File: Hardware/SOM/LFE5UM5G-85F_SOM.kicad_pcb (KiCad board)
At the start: 6 copper layers, 67.6 x 25.4 mm, 131 parts, among them J1 SODIMM-200_Split, U1 LFE5UM5G-85F, U2 AS4C256M16D3, U3 W25Q128JVP, U4 TPS62A02ADRL, U5 TPS62A02ADRL, U6 TPS62A02ADRL, U7 TPS62A02ADRL

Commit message: SOM: layout update
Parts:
- added C100: 10uF, Capacitor_SMD:C_0402_1005Metric, F.Cu at (87.6, 67.3)
- added C101: 22uF, Capacitor_SMD:C_0805_2012Metric, F.Cu at (90.4, 71.4)
- added C102: 22uF, Capacitor_SMD:C_0805_2012Metric, F.Cu at (90.4, 67.2)
- added C83: 1uF, Capacitor_SMD:C_0402_1005Metric, F.Cu at (90.0, 32.4)
- added C84: 100nF, Capacitor_SMD:C_0402_1005Metric, F.Cu at (90.0, 34.4)
- added C85: 100nF, Capacitor_SMD:C_0402_1005Metric, F.Cu at (90.0, 36.4)
- added C86: 100nF, Capacitor_SMD:C_0402_1005Metric, F.Cu at (90.0, 38.3)
- added C87: 100nF, Capacitor_SMD:C_0402_1005Metric, F.Cu at (90.0, 40.3)
- added C88: 1uF, Capacitor_SMD:C_0402_1005Metric, F.Cu at (92.9, 32.4)
- added C89: 100nF, Capacitor_SMD:C_0402_1005Metric, F.Cu at (92.9, 34.4)
- added C90: 22pF, Capacitor_SMD:C_0402_1005Metric, F.Cu at (92.9, 36.4)
- added C91: 22pF, Capacitor_SMD:C_0402_1005Metric, F.Cu at (92.9, 38.3)
- added C92: 22pF, Capacitor_SMD:C_0402_1005Metric, F.Cu at (92.9, 40.3)
- added C93: 100nF, Capacitor_SMD:C_0402_1005Metric, F.Cu at (95.8, 32.4)
- added C94: 10uF, Capacitor_SMD:C_0402_1005Metric, F.Cu at (95.8, 34.4)
- added C95: 10uF, Capacitor_SMD:C_0402_1005Metric, F.Cu at (87.6, 79.5)
- added C96: 10uF, Capacitor_SMD:C_0402_1005Metric, F.Cu at (87.6, 75.5)
- added C97: 22uF, Capacitor_SMD:C_0805_2012Metric, F.Cu at (90.5, 79.4)
- added C98: 22uF, Capacitor_SMD:C_0805_2012Metric, F.Cu at (90.5, 75.5)
- added C99: 10uF, Capacitor_SMD:C_0402_1005Metric, F.Cu at (87.6, 71.4)
- added FB4: FerriteBead, Inductor_SMD:L_1206_3216Metric, F.Cu at (85.7, 33.1)
- added FB5: FerriteBead, Inductor_SMD:L_1206_3216Metric, F.Cu at (85.7, 36.6)
- added FB6: FerriteBead, Inductor_SMD:L_1206_3216Metric, F.Cu at (85.7, 40.0)
- added FB7: FerriteBead, Inductor_SMD:L_1206_3216Metric, F.Cu at (85.7, 43.5)
- added FB8: FerriteBead, Inductor_SMD:L_0402_1005Metric, F.Cu at (85.7, 47.0)
- added FB9: FerriteBead, Inductor_SMD:L_0402_1005Metric, F.Cu at (85.7, 50.4)
- C1, C14, C18, C22, C30, C31, C34, C35, C39, C5, C9: moved to B.Cu
- C40, C63: value 1uF -> 10uF
- C41, C42, C56, C57: value 100nF -> 10uF
- C44, C45: value 100nF -> 1uF
- C48, C68: value 1uF -> 100nF
- C54, C75, C76: value 10uF -> 100nF
- C55, C74, C80: value 10uF -> 1uF
- C58, C59: value 22uF -> 10uF; footprint Capacitor_SMD:C_0805_2012Metric -> Capacitor_SMD:C_0402_1005Metric
- C70, C72: value 22pF -> 1uF
- C71: value 22pF -> 100nF
- C77: value 22uF -> 100nF; footprint Capacitor_SMD:C_0805_2012Metric -> Capacitor_SMD:C_0402_1005Metric
- C79: value 10uF -> 22uF; footprint Capacitor_SMD:C_0402_1005Metric -> Capacitor_SMD:C_0805_2012Metric
- C81, C82: value 22uF -> 1uF; footprint Capacitor_SMD:C_0805_2012Metric -> Capacitor_SMD:C_0402_1005Metric
- FB2, FB3: footprint Inductor_SMD:L_0402_1005Metric -> Inductor_SMD:L_1206_3216Metric
- moved C30 76.0 mm to (115.5, 74.2), turned to 90 degrees
- moved C22 67.5 mm to (114.3, 68.9), turned to 90 degrees
- moved C31 66.6 mm to (115.3, 68.1), turned to -90 degrees
- moved C1 65.1 mm to (114.3, 70.9), turned to 90 degrees
- moved C9 64.6 mm to (117.5, 74.2), turned to 90 degrees
- moved C5 63.1 mm to (116.5, 74.2), turned to 90 degrees
- moved C14 62.1 mm to (117.1, 72.2), turned to -90 degrees
- moved C18 60.4 mm to (118.5, 72.4), turned to 180 degrees
- moved C39 56.5 mm to (118.4, 68.1), turned to -90 degrees
- moved C34 55.1 mm to (114.5, 74.2), turned to 90 degrees
- moved C35 55.1 mm to (115.6, 72.3), turned to 180 degrees
- moved C77 42.4 mm to (48.3, 75.1)
- moved C59 26.0 mm to (166.8, 55.0)
- moved FB2 24.0 mm to (158.6, 50.4)
- moved FB3 23.4 mm to (158.4, 53.5)
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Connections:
- C15 pad 2: Net-(C15-Pad2) -> 3.3V
- C19 pad 2: Net-(C15-Pad2) -> 3.3V
- C24 pad 2: Net-(C15-Pad2) -> 3.3V
- C40 pad 2: DDR_VREF -> VCCA0
- C41 pad 2: DDR_VREF -> VCCHTX0
- C42 pad 2: 2.5V_A -> VCC_SER_0
- C43 pad 2: DDR_VREF -> VCCA0
- C44 pad 2: 2.5V_A -> VCCHTX0
- C45 pad 2: DDR_VREF -> VCC_SER_0
- C47 pad 2: 2.5V_A -> VCCA0
- C48 pad 2: DDR_VREF -> VCCHTX0
- C49 pad 2: 2.5V_A -> VCC_SER_0
- C50 pad 2: DDR_VREF -> 2.5V_A
- C51 pad 2: 2.5V_A -> VCCA0
- C52 pad 2: 2.5V_A -> VCCHTX0
- C53 pad 2: 2.5V_A -> VCC_SER_0
- C56 pad 2: DDR_VDDQ_1.5V -> VCCA1
- C57 pad 2: DDR_VDD_1.5V -> VCCHTX1
- C58 pad 2: DDR_VDDQ_1.5V -> VCC_SER_1
- C59 pad 2: DDR_VDD_1.5V -> 2.5V_A
- C60 pad 2: DDR_VDDQ_1.5V -> VCCA1
- C61 pad 2: DDR_VDD_1.5V -> VCCHTX1
- C62 pad 2: DDR_VDDQ_1.5V -> VCC_SER_1
- C63 pad 2: DDR_VDD_1.5V -> 2.5V_A
- C64 pad 2: DDR_VDDQ_1.5V -> VCCA1
- C65 pad 2: DDR_VDD_1.5V -> VCCHTX1
- C66 pad 2: DDR_VDDQ_1.5V -> VCC_SER_1
- C67 pad 2: DDR_VDD_1.5V -> VCCA1
- C68 pad 2: DDR_VREF -> VCCHTX1
- C69 pad 2: DDR_VREF -> VCC_SER_1
- C70 pad 1: Net-(U3-~{CS}) -> GND
- C70 pad 2: GND -> DDR_VREF
- C71 pad 1: Net-(U3-CLK) -> GND
- C71 pad 2: GND -> DDR_VREF
- C72 pad 1: QSPI_MOSI/DQ0 -> GND
- C72 pad 2: GND -> DDR_VREF
- C73 pad 2: 3.3V -> DDR_VREF
- C74 pad 2: 3.3V -> DDR_VREF
- C75 pad 2: 5V -> DDR_VREF
- C76 pad 2: 5V -> DDR_VDDQ_1.5V
- C77 pad 2: 3.3V -> DDR_VDD_1.5V
- C78 pad 2: 2.5V -> DDR_VDDQ_1.5V
- C79 pad 2: 5V -> DDR_VDD_1.5V
- C80 pad 2: 5V -> DDR_VDDQ_1.5V
- C81 pad 2: 1.5V -> DDR_VDD_1.5V
- C82 pad 2: 1.2V -> DDR_VDDQ_1.5V
- FB1 pad 1: 2.5V -> 1.2V
- FB1 pad 2: 2.5V_A -> VCCA0
- FB2 pad 1: 1.5V -> 1.2V
- FB2 pad 2: DDR_VDDQ_1.5V -> VCCHTX0
- FB3 pad 1: 1.5V -> 1.2V
- FB3 pad 2: DDR_VDD_1.5V -> VCC_SER_0
- R1 pad 1: DDR_CKE -> /DDR/DDR_CKE
- R1 pad 2: DDR_NCK -> /DDR/DDR_NCK
- U1 pad F11: 1.5V -> 3.3V
- U1 pad F12: 1.5V -> 3.3V
- U1 pad F17: DDR_CKE -> DDR_CK_P
- U1 pad G18: DDR_NCK -> DDR_CK_N
- U1 pad T10: Net-(U1A-VCCHTX1_D0CH1) -> VCCHTX1
- U1 pad T11: Net-(U1A-VCCHTX0_D0CH0) -> VCCHTX0
- U1 pad T12: Net-(U1A-VCCHRX0_D0CH0) -> VCC_SER_0
- U1 pad T13: Net-(U1A-VCCHRX1_D0CH1) -> VCC_SER_1
- U1 pad T14: Net-(U1A-VCCHTX1_D0CH1) -> VCCHTX1
- U1 pad T15: 2.5V_A -> VCCA1
- U1 pad T6: 2.5V_A -> VCCA0
- U1 pad T7: Net-(U1A-VCCHTX0_D0CH0) -> VCCHTX0
- U1 pad T8: Net-(U1A-VCCHRX0_D0CH0) -> VCC_SER_0
- U1 pad T9: Net-(U1A-VCCHRX1_D0CH1) -> VCC_SER_1
- U1 pad U15: 2.5V_A -> VCCA1
- U1 pad U6: 2.5V_A -> VCCA0
- U2 pad K7: DDR_NCK -> DDR_CK_N
- U2 pad K9: DDR_CKE -> DDR_CK_P
- U5 pad 4: unconnected-(U5-EN-Pad4) -> /Power Supply/1.5V_PG
- U6 pad 4: unconnected-(U6-EN-Pad4) -> BB_PGOOD
- U6 pad 6: unconnected-(U6-PG-Pad6) -> /Power Supply/1.5V_PG
- U7 pad 4: unconnected-(U7-EN-Pad4) -> /Power Supply/1.5V_PG
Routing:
- net GND: track 90.9 -> 124.8 mm, vias 30 -> 62
- net 1.2V: track 2.04 -> 31.4 mm, vias 0 -> 12
- net DDR_UDQS_P: track 1.23 -> 24.3 mm
- net DDR_UDQS_N: track 1.23 -> 22.8 mm
- net DDR_LDQS_N: track 1.35 -> 21.5 mm
- net (no net): track 18.9 -> 0.00 mm, vias 3 -> 0
- net DDR_LDQS_P: track 1.36 -> 20.2 mm
- net DDR_DQ14: track 0.00 -> 18.2 mm, vias 0 -> 2
- net DDR_DQ8: track 0.00 -> 17.3 mm, vias 0 -> 2
- net DDR_DQ12: track 0.00 -> 17.2 mm
- net DDR_DQ9: track 0.00 -> 14.9 mm, vias 0 -> 2
- net DDR_DQ15: track 0.00 -> 14.4 mm, vias 0 -> 2
- net DDR_DQ13: track 0.00 -> 13.4 mm, vias 0 -> 3
- net DDR_DQ11: track 0.00 -> 13.4 mm, vias 0 -> 2
- net DDR_VREF: track 0.00 -> 12.6 mm, vias 0 -> 2
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- added copper zone on In4.Cu, net DDR_VDDQ_1.5V
- added copper zone on In4.Cu, net DDR_VDD_1.5V

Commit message: SOM: layout update
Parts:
- C46, C50, C54, C55, C59, C63, C72, C73, C74, C75: moved to B.Cu
- moved C77 95.6 mm to (143.9, 74.1), turned to 180 degrees
- moved C71 78.8 mm to (127.5, 62.7), turned to -90 degrees
- moved C70 77.8 mm to (126.4, 62.7), turned to -90 degrees
- moved C79 73.1 mm to (144.5, 75.7)
- moved C74 72.3 mm to (120.5, 74.3), turned to 90 degrees
- moved C78 70.3 mm to (144.5, 69.7), turned to 180 degrees
- moved C80 68.6 mm to (143.8, 68.2)
- moved R9 68.0 mm to (130.4, 70.6), turned to 180 degrees
- moved FB2 66.9 mm to (94.8, 70.5)
- moved R10 65.2 mm to (128.8, 69.1), turned to -90 degrees
- moved C82 65.2 mm to (139.9, 62.2), turned to 180 degrees
- moved FB3 65.2 mm to (94.8, 67.9)
- moved C72 64.5 mm to (112.7, 69.4), turned to -90 degrees
- moved C83 64.0 mm to (143.8, 67.1), turned to 180 degrees
- moved C73 62.7 mm to (111.2, 69.4), turned to -90 degrees
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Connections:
- J1 pad 10: unconnected-(J1-Pad10) -> 5V
- J1 pad 14: unconnected-(J1-Pad14) -> GND
- J1 pad 16: unconnected-(J1-Pad16) -> GND
- J1 pad 18: unconnected-(J1-Pad18) -> GND
- J1 pad 2: unconnected-(J1-Pad2) -> 5V
- J1 pad 20: unconnected-(J1-Pad20) -> GND
- J1 pad 22: unconnected-(J1-Pad22) -> GND
- J1 pad 4: unconnected-(J1-Pad4) -> 5V
- J1 pad 6: unconnected-(J1-Pad6) -> 5V
- J1 pad 8: unconnected-(J1-Pad8) -> 5V
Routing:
- net GND: track 124.8 -> 188.2 mm, vias 62 -> 97
- net 5V: track 32.5 -> 48.6 mm, vias 0 -> 10
- net DDR_VDDQ_1.5V: track 12.0 -> 26.5 mm
- net DDR_VREF: track 12.6 -> 26.8 mm, vias 2 -> 4
- net DDR_VDD_1.5V: track 11.0 -> 20.8 mm, vias 5 -> 4
- net 2.5V_A: track 0.57 -> 9.63 mm, vias 1 -> 6
- net 2.5V: track 2.03 -> 3.94 mm
- net VCCA1: track 0.00 -> 0.80 mm
- net VCCA0: track 0.00 -> 0.80 mm
- added copper zone on F.Cu, net 5V
- added copper zone on F.Cu, net GND

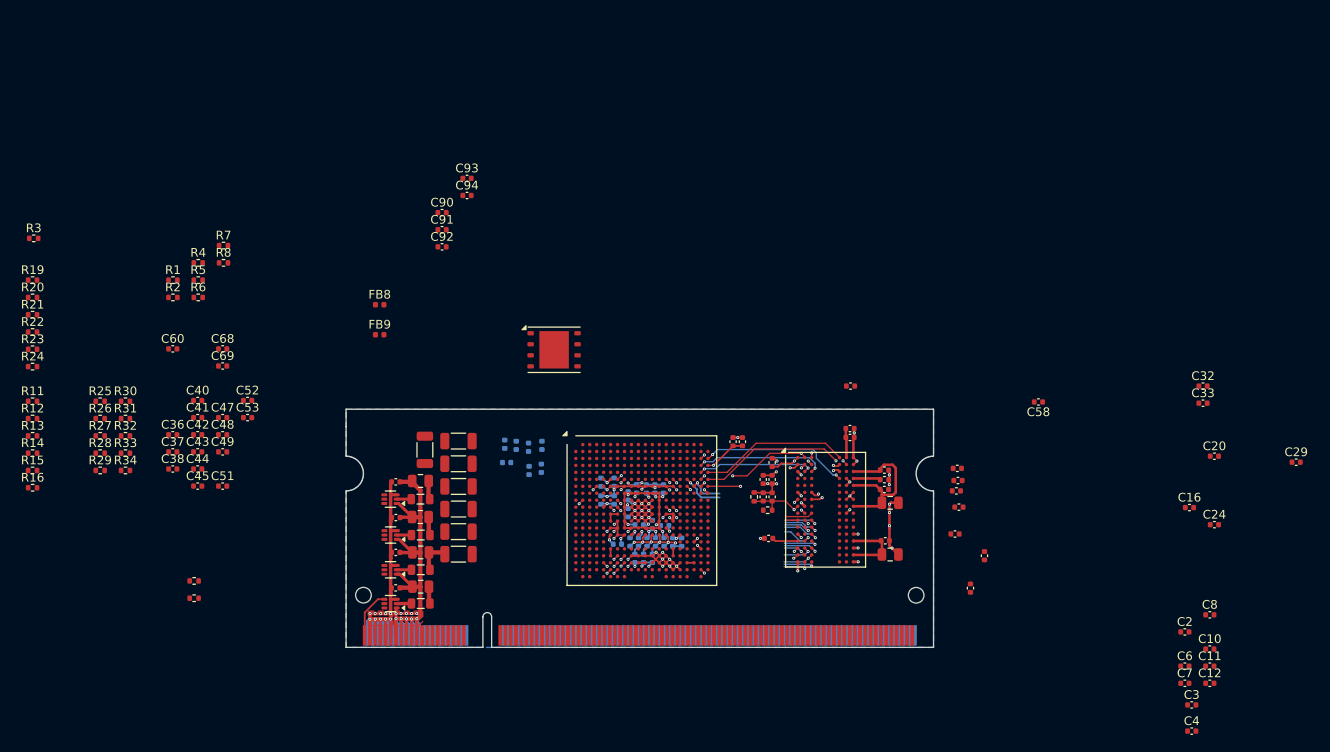
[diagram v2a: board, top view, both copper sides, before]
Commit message: SOM: QSPI layout update
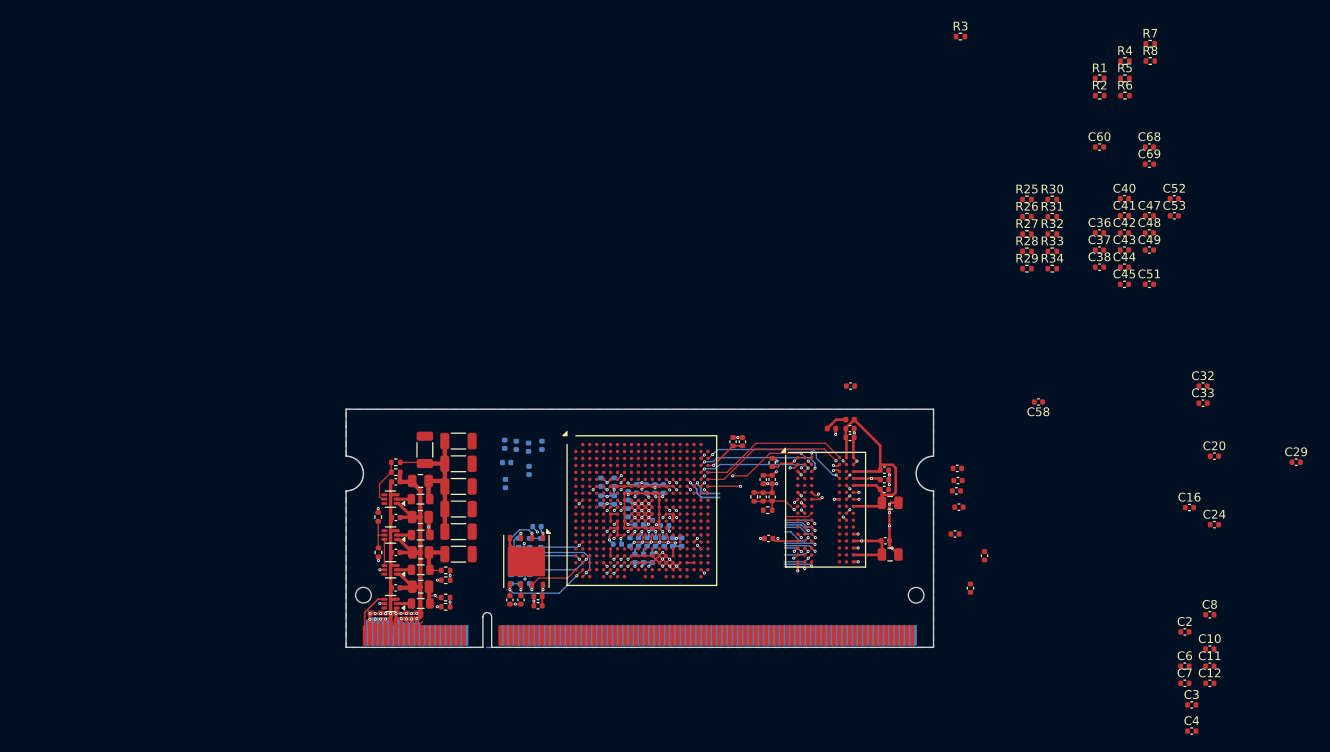
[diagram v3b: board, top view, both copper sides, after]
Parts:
- C90, R11, R12, R13, R14, R15, R16: moved to B.Cu
- moved C40 109.1 mm to (171.4, 34.8)
- moved C41 109.1 mm to (171.4, 36.7)
- moved C42 109.1 mm to (171.4, 38.7)
- moved C43 109.1 mm to (171.4, 40.7)
- moved C44 109.1 mm to (171.4, 42.6)
- moved C45 109.1 mm to (171.4, 44.6)
- moved C47 109.1 mm to (174.3, 36.7)
- moved C48 109.1 mm to (174.3, 38.7)
- moved C49 109.1 mm to (174.3, 40.7)
- moved C51 109.1 mm to (174.3, 44.6)
- moved C52 109.1 mm to (177.2, 34.8)
- moved C53 109.1 mm to (177.2, 36.7)
- moved C68 109.1 mm to (174.3, 28.8)
- moved C69 109.1 mm to (174.3, 30.8)
- moved R1 109.1 mm to (168.6, 20.9)
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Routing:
- net 3.3V: track 5.08 -> 43.5 mm, vias 2 -> 6
- net DDR_VDD_1.5V: track 20.8 -> 58.1 mm, vias 4 -> 10
- net 1.2V: track 31.4 -> 50.5 mm
- net QSPI_WP/DQ2: track 0.00 -> 15.1 mm, vias 0 -> 2
- net QSPI_MISO/DQ1: track 0.00 -> 13.9 mm, vias 0 -> 2
- net QSPI_MOSI/DQ0: track 0.00 -> 10.9 mm, vias 0 -> 2
- net 1.5V: track 7.01 -> 17.4 mm, vias 3 -> 5
- net Net-(U5-FB): track 0.00 -> 10.0 mm, vias 0 -> 2
- net QSPI_CLK: track 0.00 -> 9.96 mm, vias 0 -> 1
- net Net-(U4-FB): track 0.00 -> 9.74 mm, vias 0 -> 2
- net GND: track 188.2 -> 197.1 mm, vias 97 -> 105
- net DDR_VDDQ_1.5V: track 26.5 -> 35.3 mm
- net QSPI_RST/DQ3: track 0.00 -> 7.13 mm, vias 0 -> 1
- net Net-(U7-FB): track 0.00 -> 5.18 mm
- net QSPI_CS: track 0.00 -> 5.09 mm, vias 0 -> 1
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
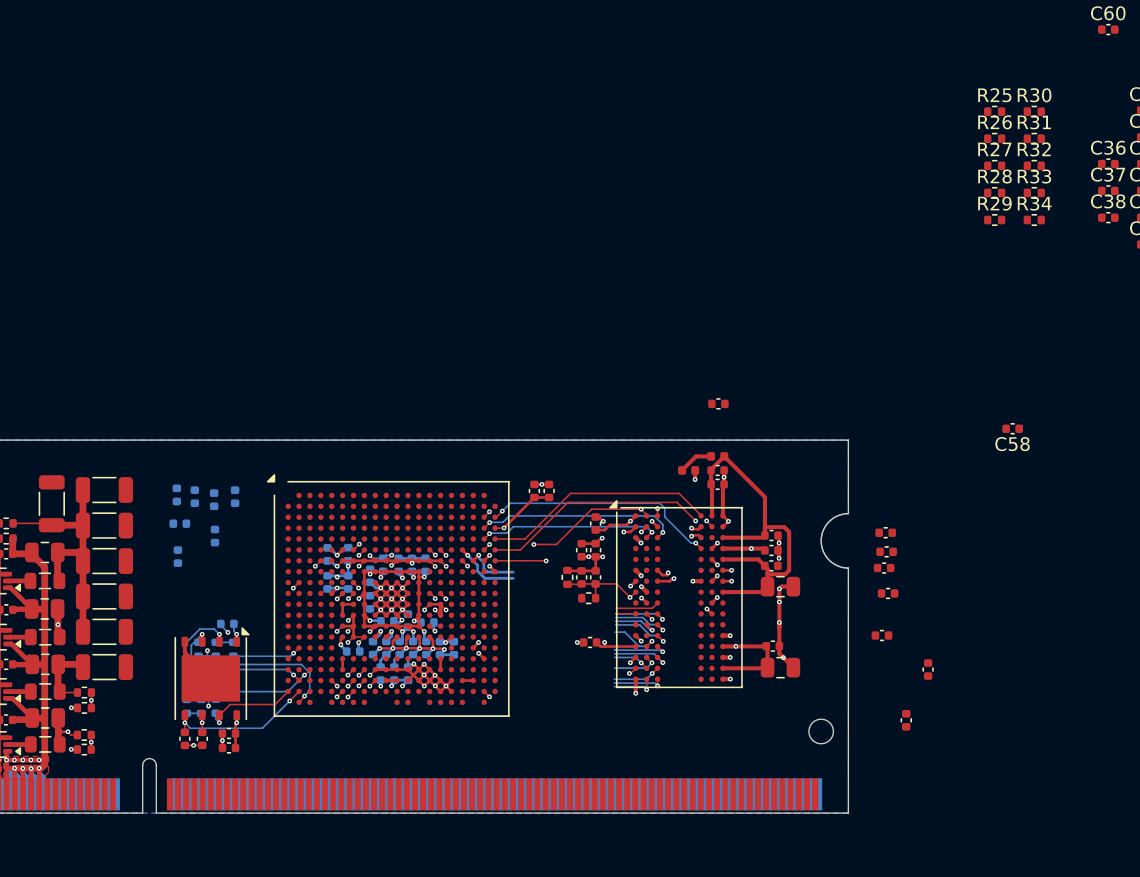
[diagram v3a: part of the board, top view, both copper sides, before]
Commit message: SOM: layout update (QSPI+
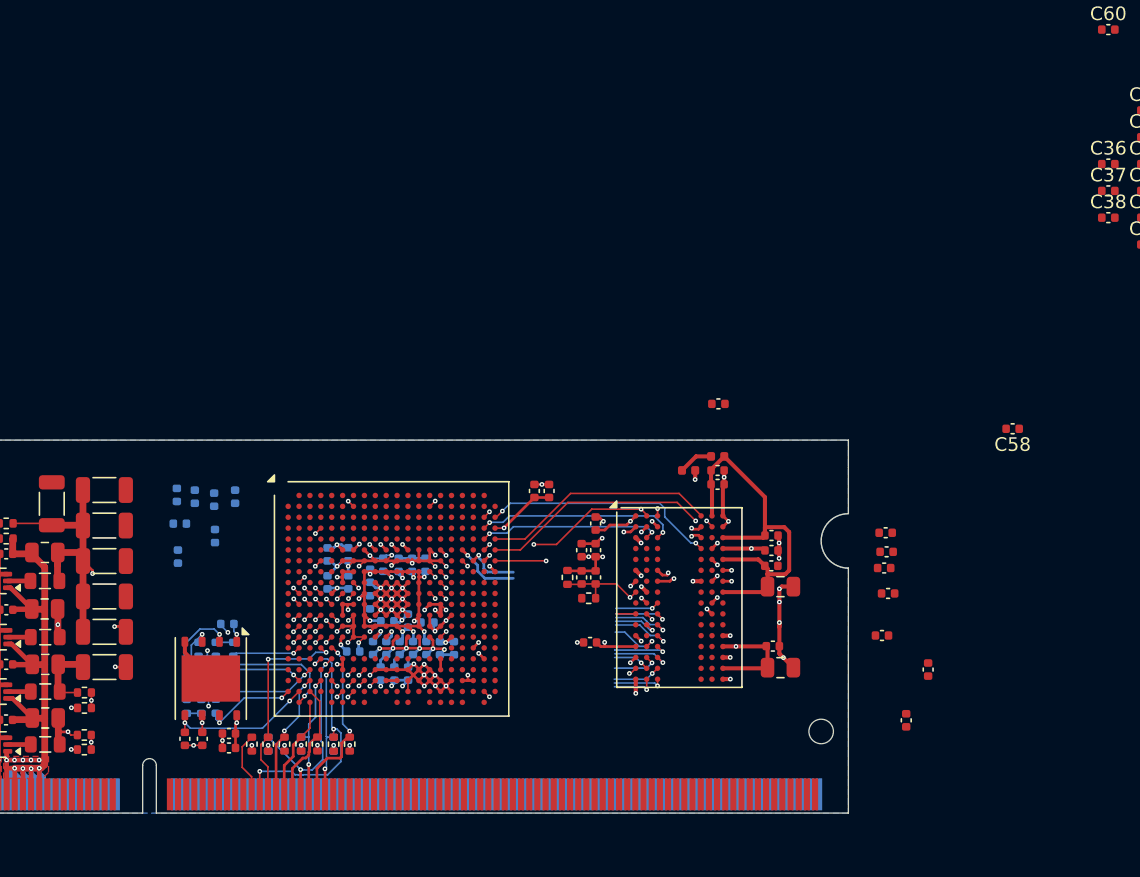
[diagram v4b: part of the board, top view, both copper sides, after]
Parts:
- R31, R33, R34: moved to B.Cu
- moved R30 73.9 mm to (105.6, 81.3), turned to 90 degrees
- moved R31 69.9 mm to (109.3, 81.3), turned to -90 degrees
- moved R26 68.6 mm to (108.0, 81.3), turned to 90 degrees
- moved R34 68.2 mm to (106.8, 81.3), turned to -90 degrees
- moved R25 68.1 mm to (110.5, 81.3), turned to 90 degrees
- moved R27 66.3 mm to (109.3, 81.3), turned to 90 degrees
- moved R32 65.8 mm to (112.8, 81.3), turned to -90 degrees
- moved R29 65.8 mm to (106.8, 81.3), turned to 90 degrees
- moved R33 65.5 mm to (111.7, 81.3), turned to -90 degrees
- moved R28 63.2 mm to (111.7, 81.3), turned to 90 degrees
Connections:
- C10 pad 2: Net-(C10-Pad2) -> 3.3V
- C16 pad 2: Net-(C16-Pad2) -> 3.3V
- C17 pad 2: Net-(C17-Pad2) -> 3.3V
- C2 pad 2: Net-(C10-Pad2) -> 3.3V
- C20 pad 2: Net-(C16-Pad2) -> 3.3V
- C21 pad 2: Net-(C17-Pad2) -> 3.3V
- C25 pad 2: Net-(C16-Pad2) -> 3.3V
- C26 pad 2: Net-(C17-Pad2) -> 3.3V
- C29 pad 2: Net-(C29-Pad2) -> 3.3V
- C33 pad 2: Net-(C29-Pad2) -> 3.3V
- C37 pad 2: Net-(C29-Pad2) -> 3.3V
- C6 pad 2: Net-(C10-Pad2) -> 3.3V
- J1 pad 61: unconnected-(J1-Pad61) -> BOOT_MODE_0
- J1 pad 63: unconnected-(J1-Pad63) -> BOOT_MODE_1
- J1 pad 65: unconnected-(J1-Pad65) -> BOOT_MODE_2
- J1 pad 67: unconnected-(J1-Pad67) -> INIT#
- J1 pad 69: unconnected-(J1-Pad69) -> DONE
- J1 pad 71: unconnected-(J1-Pad71) -> PROGRAM#
- J1 pad 73: unconnected-(J1-Pad73) -> JTAG_TCK
- J1 pad 75: unconnected-(J1-Pad75) -> JTAG_TDO
- J1 pad 77: unconnected-(J1-Pad77) -> JTAG_TDI
- J1 pad 79: unconnected-(J1-Pad79) -> JTAG_TMS
- U1 pad F10: Net-(U1B-VCCIO0-PadF10) -> 3.3V
- U1 pad F9: Net-(U1B-VCCIO0-PadF10) -> 3.3V
- U1 pad H6: Net-(U1G-VCCIO7-PadH6) -> 3.3V
- U1 pad H7: Net-(U1G-VCCIO7-PadH6) -> 3.3V
- U1 pad J6: Net-(U1G-VCCIO7-PadH6) -> 3.3V
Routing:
- net 2.5V_A: track 9.63 -> 56.9 mm, vias 6 -> 9
- net 1.5V: track 17.4 -> 52.4 mm, vias 5 -> 9
- net 1.2V: track 50.5 -> 74.0 mm, vias 12 -> 13
- net 3.3V: track 43.5 -> 66.2 mm, vias 6 -> 16
- net VCCA0: track 0.80 -> 20.1 mm, vias 0 -> 2
- net BOOT_MODE_1: track 0.00 -> 18.5 mm, vias 0 -> 3
- net BOOT_MODE_2: track 0.00 -> 15.4 mm, vias 0 -> 2
- net JTAG_TCK: track 0.00 -> 15.0 mm, vias 0 -> 2
- net JTAG_TDI: track 0.00 -> 13.0 mm, vias 0 -> 2
- net JTAG_TMS: track 0.00 -> 9.90 mm, vias 0 -> 2
- net INIT#: track 0.00 -> 9.44 mm, vias 0 -> 2
- net GND: track 197.1 -> 206.4 mm, vias 105 -> 110
- net JTAG_TDO: track 0.00 -> 9.29 mm, vias 0 -> 2
- net PROGRAM#: track 0.00 -> 8.87 mm
- net DONE: track 0.00 -> 7.54 mm
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
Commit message: SOM: layout update
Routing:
- net DDR_RST: track 3.81 -> 33.1 mm, vias 2 -> 3
- net 3.3V: track 66.2 -> 55.1 mm
- net QSPI_RST/DQ3: track 7.36 -> 15.4 mm
- net QSPI_MOSI/DQ0: track 10.9 -> 15.2 mm
- net QSPI_CLK: track 9.96 -> 14.0 mm
- net GND: track 206.4 -> 208.0 mm, vias 110 -> 113
- net VCCHTX0: track 0.00 -> 0.56 mm, vias 0 -> 1
